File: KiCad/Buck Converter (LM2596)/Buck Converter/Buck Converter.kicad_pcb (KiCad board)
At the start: 2 copper layers, 10 parts, among them J1 Conn_01x02_Socket, J2 Conn_01x02_Socket, U1 LM2596S-ADJ

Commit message: Update Buck Converter.kicad_pcb
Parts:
- moved J1 43.9 mm to (116.0, 116.0)
- moved R1 41.1 mm to (151.2, 91.6), turned to 90 degrees
- moved R2 34.1 mm to (166.8, 91.6), turned to -90 degrees
- moved C_FF1 28.7 mm to (159.2, 89.1), turned to -90 degrees
- moved U1 24.3 mm to (141.4, 109.4)
- moved J2 22.5 mm to (189.7, 116.0)
- moved D1 21.8 mm to (143.0, 131.7), turned to 0 degrees
- moved C_OUT1 19.9 mm to (189.7, 88.3), turned to -90 degrees
- moved L1 18.0 mm to (164.2, 113.0), turned to 0 degrees
- moved C_IN1 17.3 mm to (116.0, 88.3), turned to -90 degrees
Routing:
- net Net-(J2-Pin_2): track 0.00 -> 80.5 mm
- net Net-(J1-Pin_2): track 0.00 -> 65.4 mm
- net Net-(U1-FB): track 0.00 -> 58.3 mm
- net Net-(D1-K): track 0.00 -> 47.1 mm
- added copper zone on F.Cu, net GND
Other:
- board outline added: 100.8 x 73.6 mm

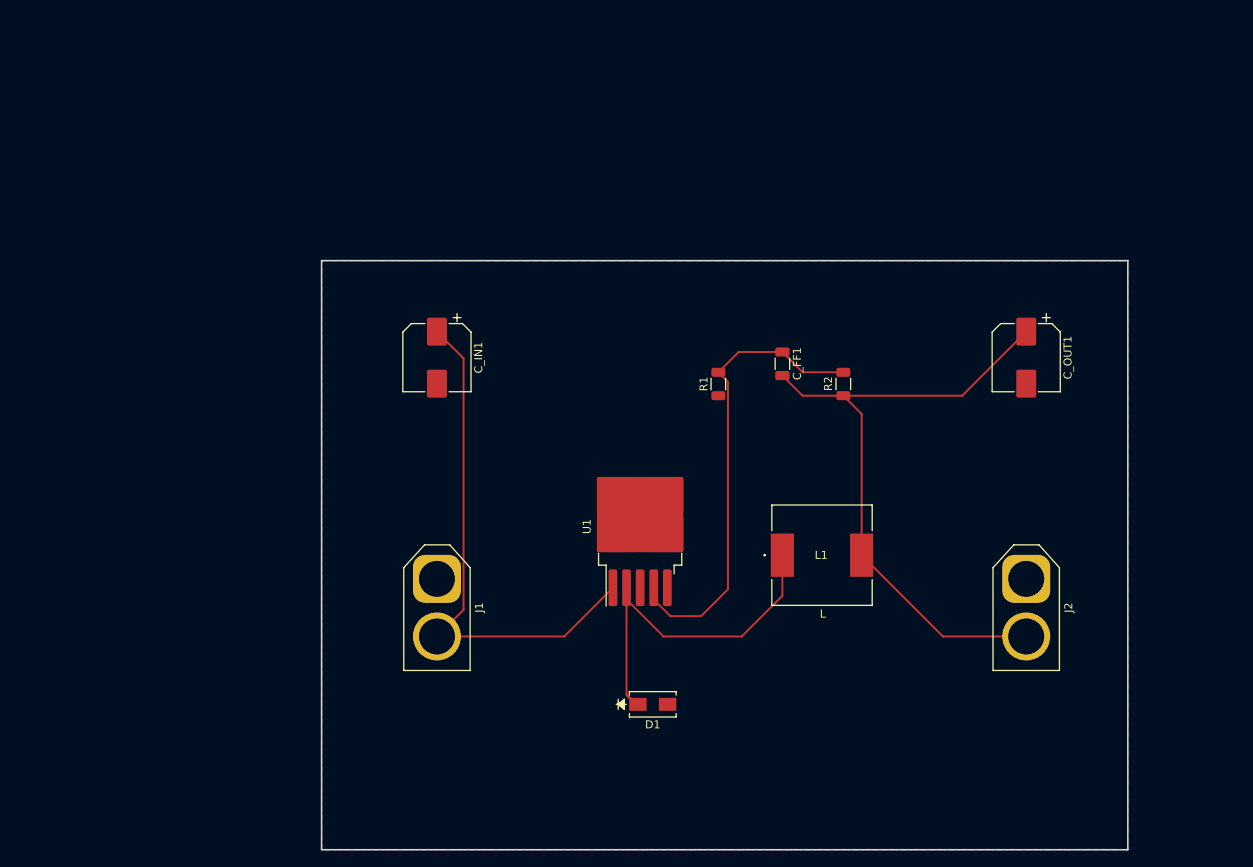
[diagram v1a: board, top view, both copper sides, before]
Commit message: update buck dimensions
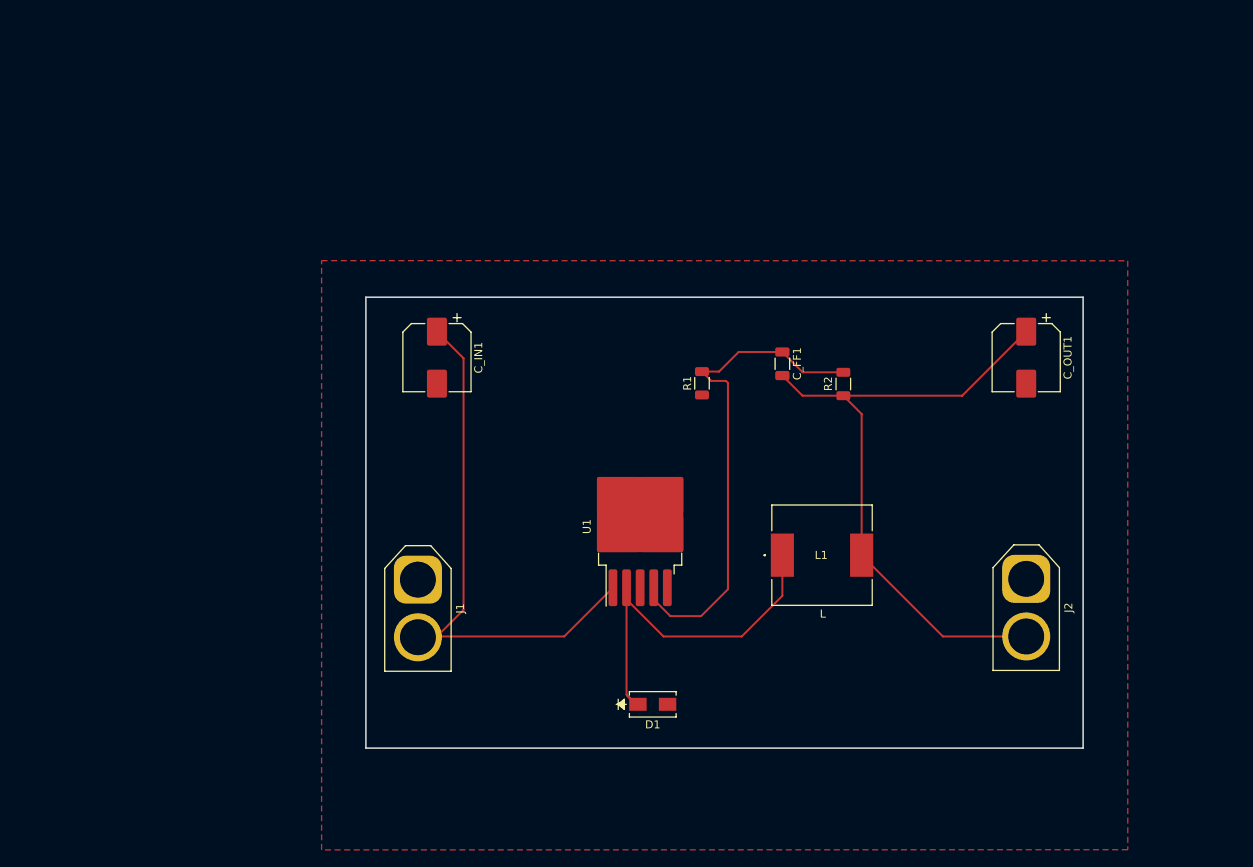
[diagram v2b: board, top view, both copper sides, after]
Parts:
- moved J1 2.38 mm to (113.6, 116.1)
- moved R1 2.05 mm to (149.1, 91.5)
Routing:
- net Net-(J1-Pin_2): track 65.4 -> 70.2 mm
- net Net-(U1-FB): track 58.3 -> 62.4 mm
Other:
- board size 100.8 x 73.6 mm -> 89.7 x 56.4 mm
